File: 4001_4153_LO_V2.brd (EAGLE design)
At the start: 109 x 63 mm, 108 parts, among them IC1 74LVC2G17GV,125, IC10 MCP6H01, IC2 74LVC2G17GV,125, IC3 74LVC2G17GV,125, IC4 ADF4001BRUZ, IC5 ATTINY45V-10SU, IC6 7805DT, IC7 7809DT, IC8 LD117ASTR, IC9 ADF4153BRUZ-RL7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

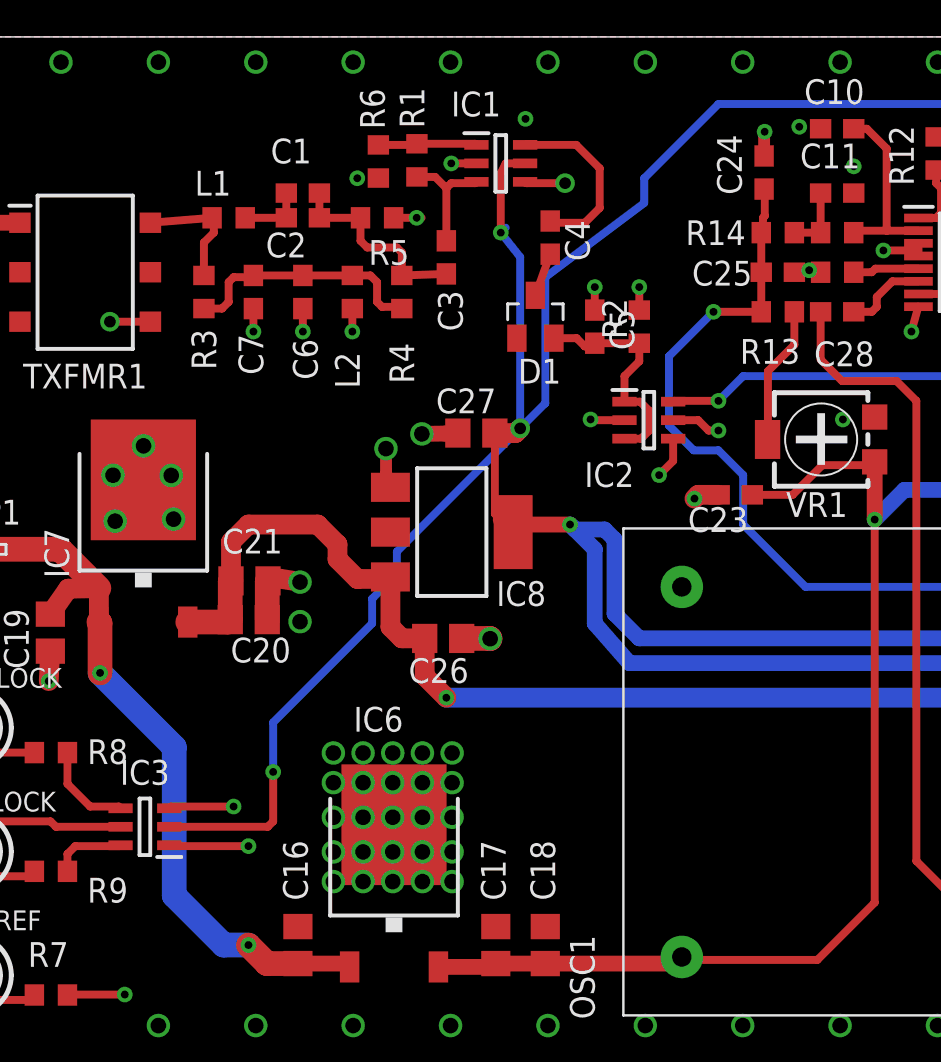
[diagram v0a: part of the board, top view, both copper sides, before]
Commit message: Misc circuit revisions
Updated loop filter on 4001, added pullups to MUXOUT
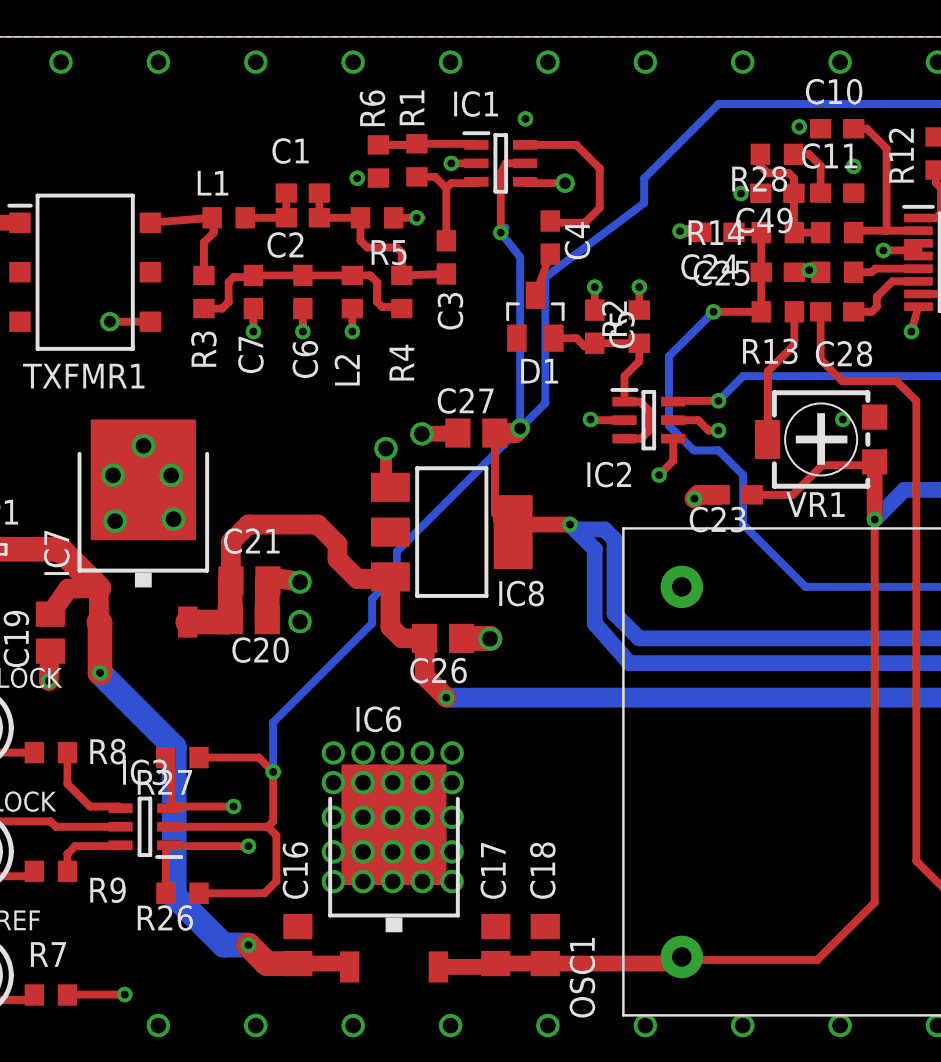
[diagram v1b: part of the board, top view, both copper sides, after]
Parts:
- added C49: 10nF, resistor:C0603
- added R26, R27: 10K, rcl:R0603
- added R28: 150R, rcl:R0603
- moved C24 3.89 mm to (43.5, 43.0), turned to 180 degrees
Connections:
- new net N$22: C11.1, R28.1
- net +3V3: now also R26.1, R27.1
- net 4001_CP: now also C49.1, R28.2; no longer C11.1
- net GND: now also C49.2
- net MUX2: now also R26.2
- net N$26: now also R27.2
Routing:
- net +3V3: track 267.4 -> 278.8 mm
- net 4001_CP: track 3.38 -> 6.73 mm
- net N$22: track 0.00 -> 3.04 mm
- net N$26: track 66.0 -> 68.6 mm
- net MUX2: track 62.1 -> 64.7 mm
- net GND: track 68.4 -> 68.3 mm, vias 184 -> 185
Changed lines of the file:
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@@
 <setting verticaltext="up"/>
 </settings>
-<grid distance="1" unitdist="mm" unit="mm" style="lines" multiple="1" display="no" altdistance="0.01" altunitdist="inch" altunit="inch"/>
+<grid distance="1" unitdist="mm" unit="mm" style="lines" multiple="1" display="no" altdistance="0.001" altunitdist="inch" altunit="inch"/>
 <layers>
 <layer number="1" name="Top" color="4" fill="1" visible="yes" active="yes"/>
@@
 <attribute name="VALUE" x="83.031778125" y="16.751146875" size="1.27" layer="27" rot="R270"/>
 </element>
-<element name="C24" library="rcl" package="C0603" value="100nF" x="45.86486875" y="46.03795625" smashed="yes" rot="R90">
-<attribute name="NAME" x="44.72186875" y="44.89495625" size="1.27" layer="25" rot="R90"/>
-<attribute name="VALUE" x="47.76986875" y="45.40295625" size="1.27" layer="27" rot="R90"/>
+<element name="C24" library="rcl" package="C0603" value="100nF" x="43.47164375" y="42.96926875" smashed="yes" rot="R180">
+<attribute name="NAME" x="44.61464375" y="41.82626875" size="1.27" layer="25" rot="R180"/>
+<attribute name="VALUE" x="44.10664375" y="44.87426875" size="1.27" layer="27" rot="R180"/>
 </element>
 <element name="IC7" library="linear" package="TO252" value="7809DT" x="13.994" y="27.759" smashed="yes">
@@
 <attribute name="VALUE" x="100.035" y="34.696" size="1.27" layer="27" rot="R90"/>
 </element>
+<element name="R26" library="rcl" package="R0603" value="10K" x="16.004" y="9.034" rot="R180"/>
+<element name="R27" library="rcl" package="R0603" value="10K" x="16" y="16" rot="R180"/>
+<element name="C49" library="resistor" package="C0603" value="10nF" x="46.5468" y="44.971" rot="R180"/>
+<element name="R28" library="rcl" package="R0603" value="150R" x="46.5214" y="46.9738" rot="R180"/>
 </elements>
 <signals>
@@
 <wire x1="83.816090625" y1="23.12368125" x2="83.816090625" y2="24.22191875" width="0.6096" layer="1"/>
 <wire x1="83.816090625" y1="24.22191875" x2="83.71031875" y2="24.370146875" width="0.6096" layer="1"/>
-<via x="45.891665625" y="48.133025" extent="1-16" drill="0.4" shape="square"/>
-<wire x1="45.86486875" y1="46.88795625" x2="45.86486875" y2="48.106228125" width="0.6096" layer="1"/>
-<wire x1="45.86486875" y1="48.106228125" x2="45.891665625" y2="48.133025" width="0.6096" layer="1"/>
+<via x="41.548265625" y="43.027625" extent="1-16" drill="0.4" shape="square"/>
+<wire x1="42.62164375" y1="42.96926875" x2="42.05486875" y2="43.026228125" width="0.6096" layer="1"/>
+<wire x1="42.05486875" y1="43.026228125" x2="41.548265625" y2="43.027625" width="0.6096" layer="1"/>
 <via x="15.545871875" y="28.24148125" extent="1-16" drill="0.8" shape="square"/>
 <via x="12.43630625" y="30.496696875" extent="1-16" drill="0.8" shape="square"/>
@@
 <wire x1="59.666" y1="39.152" x2="59.666" y2="38.422690625" width="0.4064" layer="1"/>
 <wire x1="59.666" y1="38.422690625" x2="59.861665625" y2="38.227025" width="0.4064" layer="1"/>
+<contactref element="C49" pad="2"/>
+<via x="44.672465625" y="44.958025" extent="1-16" drill="0.4" shape="square"/>
 </signal>
 <signal name="+9V">
@@
 <wire x1="34.63" y1="40.665" x2="34.63" y2="34.191" width="0.4064" layer="16"/>
 <wire x1="34.63" y1="34.191" x2="33.342" y2="32.903" width="0.4064" layer="16"/>
+<contactref element="R27" pad="1"/>
+<contactref element="R26" pad="1"/>
+<wire x1="16.85" y1="16" x2="19.925" y2="16" width="0.4064" layer="1"/>
+<wire x1="19.925" y1="16" x2="20.66" y2="15.265" width="0.4064" layer="1"/>
+<wire x1="16.854" y1="9.034" x2="20.21" y2="9.034" width="0.4064" layer="1"/>
+<wire x1="20.21" y1="9.034" x2="20.828" y2="9.652" width="0.4064" layer="1"/>
+<wire x1="20.828" y1="9.652" x2="20.828" y2="12.001" width="0.4064" layer="1"/>
+<wire x1="20.828" y1="12.001" x2="20.382" y2="12.447" width="0.4064" layer="1"/>
 </signal>
 <signal name="10MHZ_REF">
@@
 <signal name="N$32">
 <contactref element="C24" pad="1"/>
-<wire x1="45.899240625" y1="45.153584375" x2="45.86486875" y2="45.18795625" width="0.4064" layer="1"/>
+<wire x1="45.238840625" y1="42.994584375" x2="44.32164375" y2="42.96926875" width="0.4064" layer="1"/>
 <contactref element="C25" pad="1"/>
 <contactref element="R14" pad="2"/>
@@
 <via x="43.266" y="38.887" extent="1-16" drill="0.4" shape="octagon"/>
 <wire x1="43.266" y1="38.887" x2="45.718" y2="38.887" width="0.4064" layer="1"/>
-<wire x1="45.899240625" y1="45.153584375" x2="45.899240625" y2="43.806240625" width="0.4064" layer="1"/>
-<wire x1="45.899240625" y1="43.806240625" x2="45.806" y2="43.713" width="0.4064" layer="1"/>
-<wire x1="45.806" y1="43.713" x2="45.806" y2="43.039" width="0.4064" layer="1"/>
+<wire x1="45.238840625" y1="42.994584375" x2="45.492840625" y2="42.917240625" width="0.4064" layer="1"/>
+<wire x1="45.492840625" y1="42.917240625" x2="45.552" y2="43.205" width="0.4064" layer="1"/>
+<wire x1="45.552" y1="43.205" x2="45.806" y2="43.039" width="0.4064" layer="1"/>
 <wire x1="45.806" y1="43.039" x2="45.718" y2="42.951" width="0.4064" layer="1"/>
 </signal>
@@
 <contactref element="R14" pad="1"/>
 <contactref element="R11" pad="2"/>
-<contactref element="C11" pad="1"/>
 <wire x1="47.418" y1="42.951" x2="48.766" y2="42.951" width="0.4064" layer="1"/>
-<wire x1="48.766" y1="42.951" x2="48.766" y2="44.983" width="0.4064" layer="1"/>
+<contactref element="R28" pad="2"/>
+<contactref element="C49" pad="1"/>
+<wire x1="47.3968" y1="44.971" x2="47.3968" y2="42.9722" width="0.4064" layer="1"/>
+<wire x1="47.3968" y1="42.9722" x2="47.418" y2="42.951" width="0.4064" layer="1"/>
+<wire x1="45.6714" y1="46.9738" x2="45.6714" y2="46.3782" width="0.4064" layer="1"/>
+<wire x1="45.6714" y1="46.3782" x2="46.0502" y2="45.9994" width="0.4064" layer="1"/>
+<wire x1="46.0502" y1="45.9994" x2="47.1424" y2="45.9994" width="0.4064" layer="1"/>
+<wire x1="47.1424" y1="45.9994" x2="47.3964" y2="45.7454" width="0.4064" layer="1"/>
+<wire x1="47.3964" y1="45.7454" x2="47.3964" y2="44.9714" width="0.4064" layer="1"/>
+<wire x1="47.3964" y1="44.9714" x2="47.3968" y2="44.971" width="0.4064" layer="1"/>
 </signal>
 <signal name="20_MHZ_4001">
@@
 <wire x1="25.74" y1="19.075" x2="27.01" y2="20.345" width="0.4064" layer="15"/>
 <wire x1="27.01" y1="20.345" x2="48.6" y2="20.345" width="0.4064" layer="15"/>
+<contactref element="R27" pad="2"/>
+<wire x1="15.414" y1="13.487" x2="15.414" y2="15.736" width="0.4064" layer="1"/>
+<wire x1="15.414" y1="15.736" x2="15.15" y2="16" width="0.4064" layer="1"/>
 </signal>
 <signal name="N$25">
@@
 <wire x1="22.438" y1="18.059" x2="67.396" y2="18.059" width="0.4064" layer="15"/>
 <wire x1="67.396" y1="18.059" x2="67.65" y2="17.805" width="0.4064" layer="15"/>
+<contactref element="R26" pad="2"/>
+<wire x1="15.154" y1="9.034" x2="15.154" y2="11.327" width="0.4064" layer="1"/>
+<wire x1="15.154" y1="11.327" x2="15.324" y2="11.497" width="0.4064" layer="1"/>
 </signal>
 <signal name="N$28">
@@
 <wire x1="98.065721875" y1="34.416721875" x2="98.13" y2="34.481" width="0.4064" layer="1"/>
 </signal>
+<signal name="N$22">
+<contactref element="C11" pad="1"/>
+<contactref element="R28" pad="1"/>
+<wire x1="47.3714" y1="46.9738" x2="48.1746" y2="46.9738" width="0.4064" layer="1"/>
+<wire x1="48.1746" y1="46.9738" x2="48.768" y2="46.3804" width="0.4064" layer="1"/>
+<wire x1="48.768" y1="46.3804" x2="48.768" y2="44.985" width="0.4064" layer="1"/>
+<wire x1="48.768" y1="44.985" x2="48.766" y2="44.983" width="0.4064" layer="1"/>
+</signal>
 </signals>

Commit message: Minor mods
Added text to rear silk,
moved a few components around the 4001 loop filter
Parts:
- moved C10 3.29 mm to (52.7, 47.0), turned to 90 degrees
- moved R28 1.50 mm to (48.0, 46.9)
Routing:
- net N$15: track 9.69 -> 6.77 mm
- net 4001_CP: track 6.73 -> 5.56 mm
- net N$22: track 3.04 -> 2.09 mm
- net +3V3: track 278.8 -> 279.6 mm
- net GND: vias 185 -> 187
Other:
- board text added: ">DRAWING_NAME"
- board text added: ">PLOT_DATE_TIME"
- board text added: "G1YFG Microwave Local Oscillator"

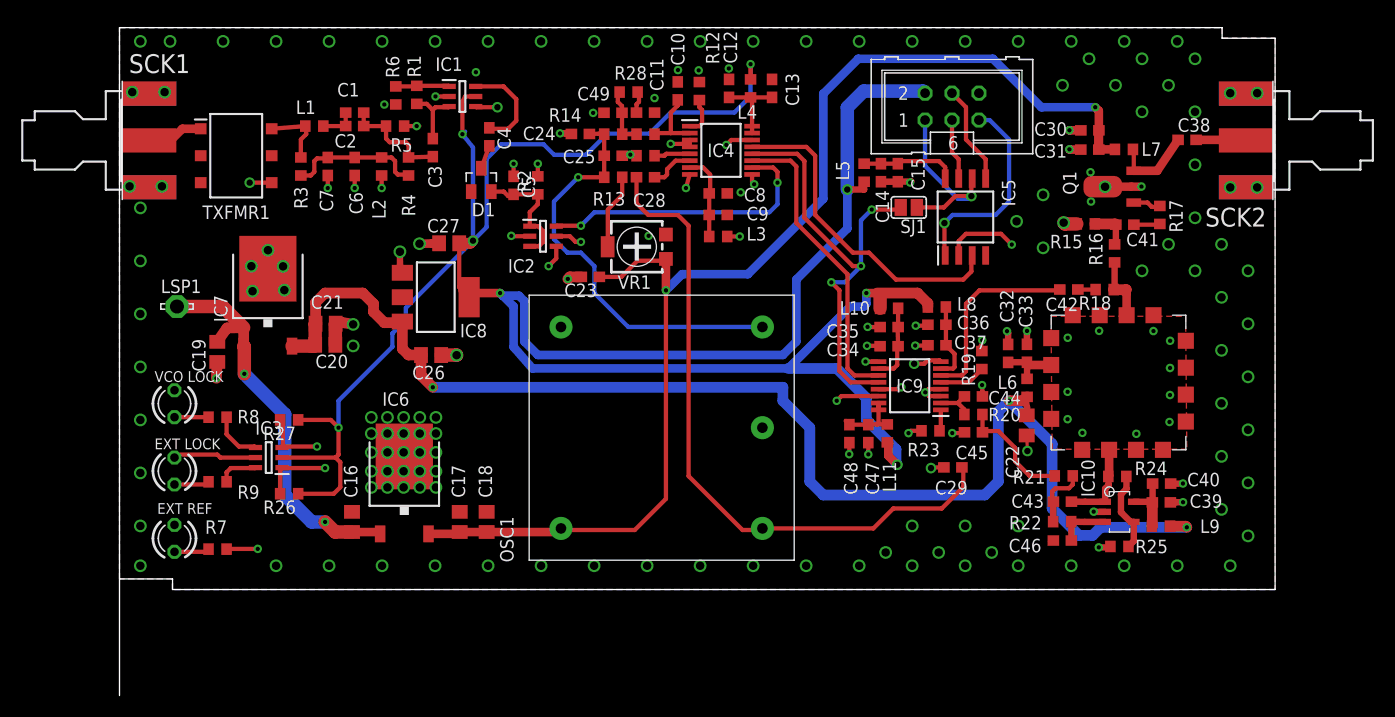
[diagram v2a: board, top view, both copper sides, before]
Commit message: Soldering mods
Moved components to clear board edges on underside for soldering to box.
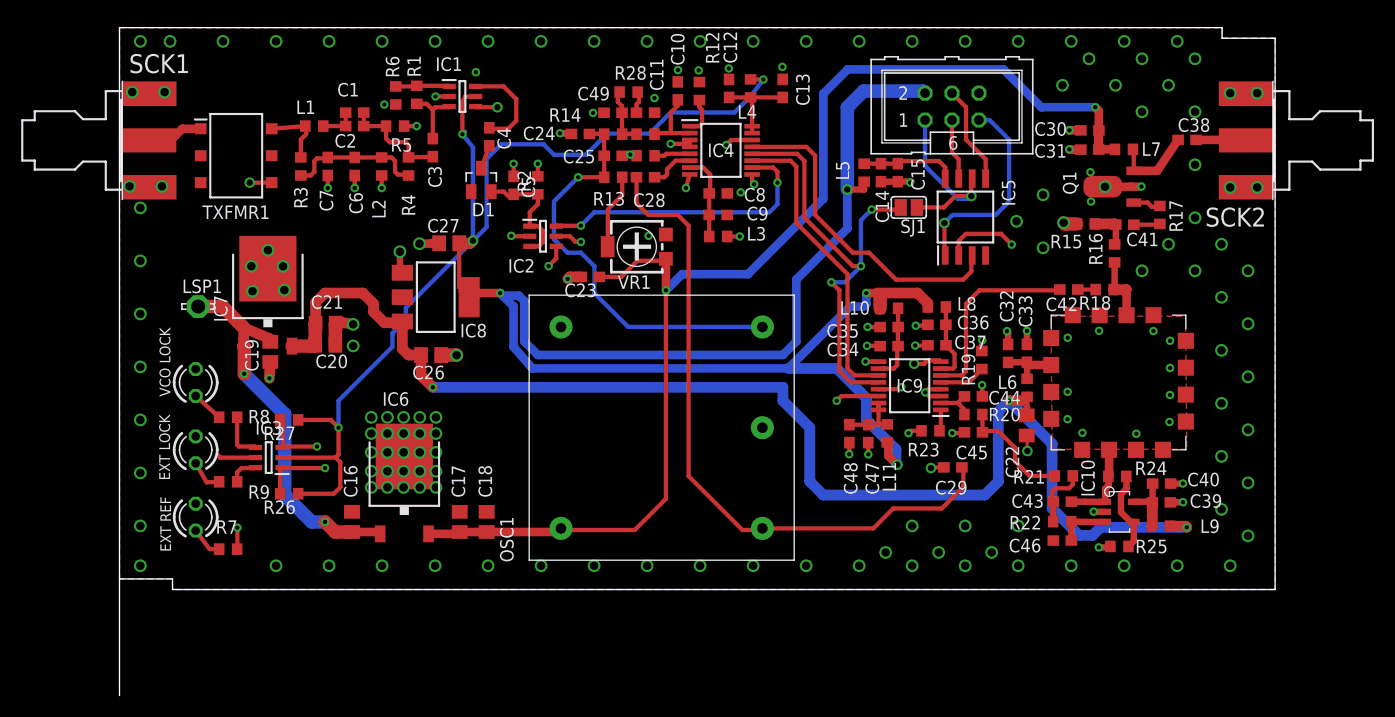
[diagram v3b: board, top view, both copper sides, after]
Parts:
- moved C19 5.00 mm to (14.2, 22.4)
- moved LED1 2.83 mm to (7.18, 6.83)
- moved LED2 2.83 mm to (7.18, 19.5)
- moved LED3 2.83 mm to (7.18, 13.2)
- moved LSP1 2.00 mm to (7.42, 26.7)
- moved C13 1.00 mm to (62.6, 47.3)
- moved R7 1.00 mm to (10.2, 3.81)
- moved R8 1.00 mm to (10.2, 16.3)
- moved R9 1.00 mm to (10.2, 10.2)
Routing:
- net GND: track 68.3 -> 64.1 mm, vias 187 -> 188
- net +3V3: track 279.6 -> 276.7 mm
- net +12V: track 38.2 -> 36.0 mm
- net N$27: track 3.80 -> 2.80 mm
- net DVDD1: track 7.49 -> 8.49 mm
- net N$29: track 51.8 -> 50.8 mm
- net +5V: track 118.2 -> 117.4 mm

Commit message: Thermal mods
Rotated 5V reg, ref  GM4ISM
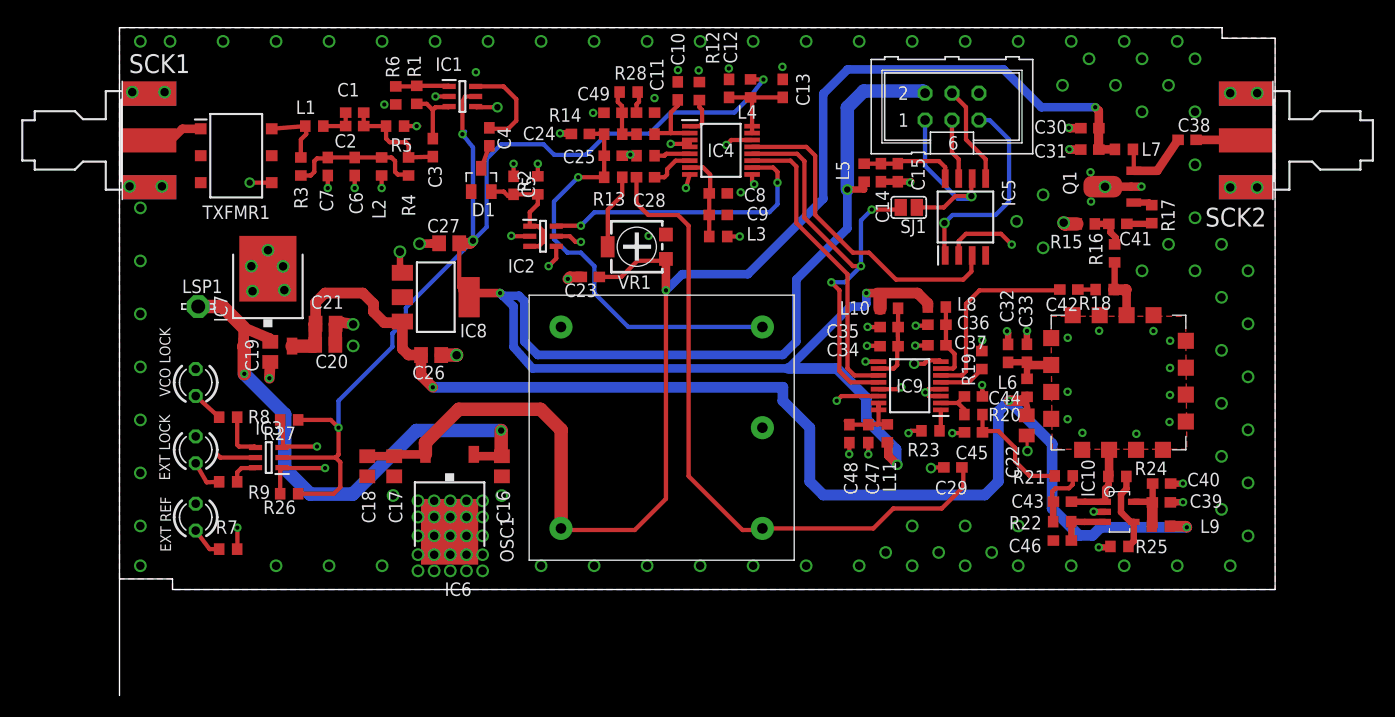
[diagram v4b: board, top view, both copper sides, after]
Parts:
- moved C16 15.1 mm to (36.1, 11.6), turned to 270 degrees
- moved C18 12.4 mm to (23.4, 11.6), turned to 270 degrees
- moved C17 8.11 mm to (25.9, 11.6), turned to 270 degrees
- moved IC6 4.76 mm to (31.1, 7.95), turned to 180 degrees
- moved R17 0.77 mm to (97.4, 35.4)
- moved C41 0.66 mm to (94.2, 34.5)
- moved C30 0.20 mm to (91.5, 43.5)
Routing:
- net +5V: track 117.4 -> 136.2 mm
- net +12V: track 36.0 -> 52.0 mm
- net N$11: track 2.67 -> 1.80 mm
